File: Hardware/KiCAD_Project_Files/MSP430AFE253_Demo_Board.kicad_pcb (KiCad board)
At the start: 2 copper layers, 25.4 x 50.8 mm, 48 parts, among them J1 USB_MINI_B, P1 POWER, P2 3.3V, P3 Spy-Bi-Wire, P4 TX, P5 RX, P6 GPIO, SW1 FSM4JH, SW2 FSM4JH, SW3 FSM4JH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

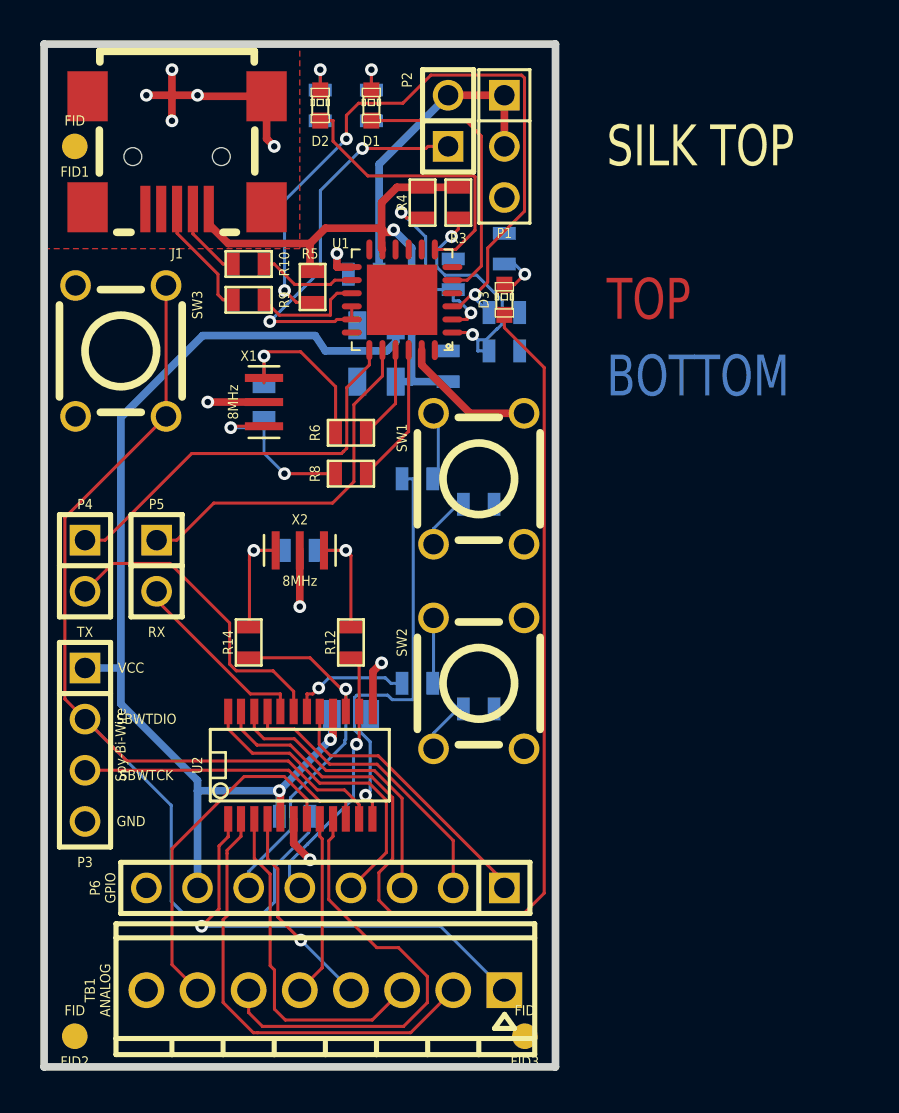
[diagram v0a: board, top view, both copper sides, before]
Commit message: The Freescale USB-to-Serial IC seems to be obsolee.  This is a baseline check-in before changing to the FTDI FT230XQ.
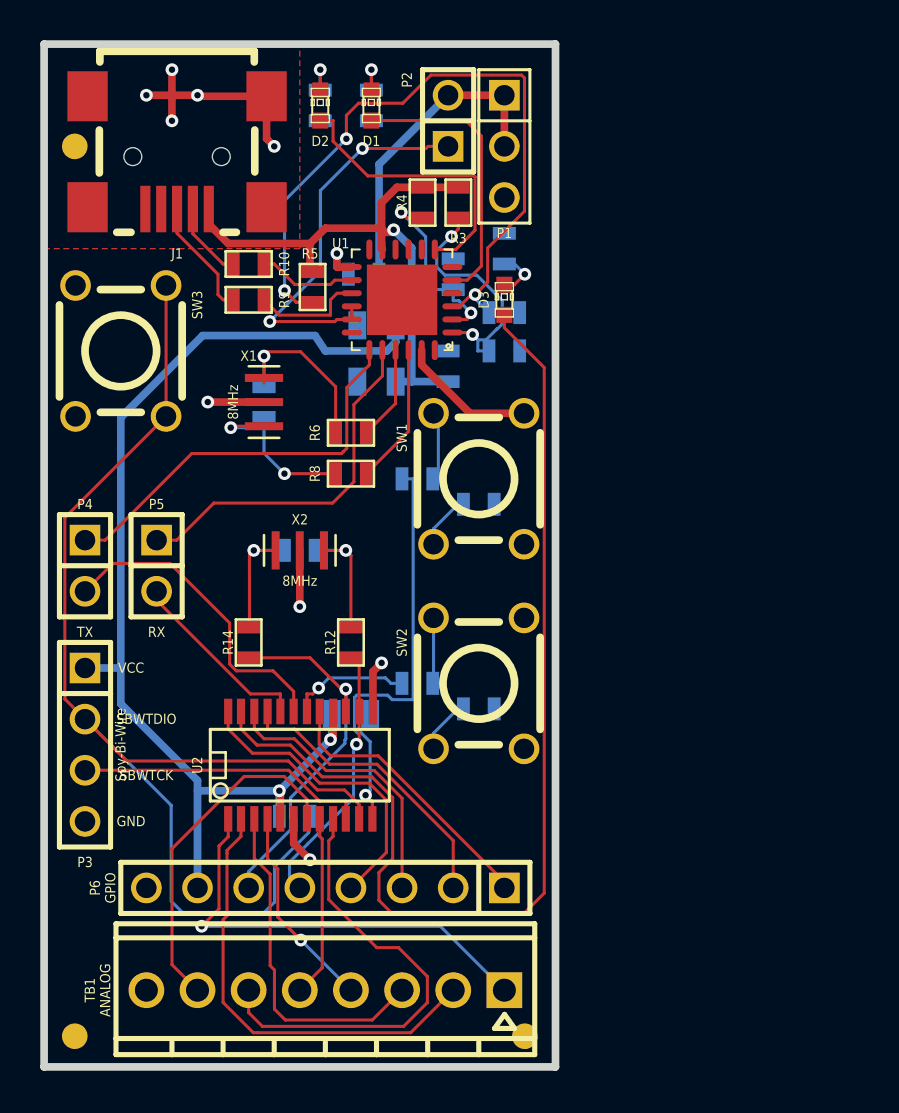
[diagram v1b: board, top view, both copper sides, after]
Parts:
- ?: renamed from FID2; value FID -> (none)
- ?: renamed from FID1; value FID -> (none)
- ?: renamed from FID3; value FID -> (none)
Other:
- board text added: "www.cascologix.com"
- board text removed: "BOTTOM"
- board text removed: "MASK BOTTOM"
- board text removed: "MASK TOP"
- board text removed: "PASTE BOTTOM"
- board text removed: "PASTE TOP"
- board text removed: "SILK BOTTOM"
- board text removed: "SILK TOP"
- board text removed: "TOP"
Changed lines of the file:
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@@
     (links 109)
     (no_connects 1)
-    (area 152.209499 75.5904 197.2564 127.2032)
+    (area 144.078476 70.8152 177.990501 127.2032)
     (thickness 1.6002)
-    (drawings 18)
+    (drawings 11)
     (tracks 448)
     (zones 0)
@@
   )
   (layers
-    (15 Front signal)
+    (15 Front signal hide)
     (0 Back signal)
-    (16 B.Adhes user)
-    (17 F.Adhes user)
-    (18 B.Paste user)
-    (19 F.Paste user)
+    (16 B.Adhes user hide)
+    (17 F.Adhes user hide)
+    (18 B.Paste user hide)
+    (19 F.Paste user hide)
     (20 B.SilkS user)
-    (21 F.SilkS user)
-    (22 B.Mask user)
-    (23 F.Mask user)
+    (21 F.SilkS user hide)
+    (22 B.Mask user hide)
+    (23 F.Mask user hide)
     (24 Dwgs.User user)
     (25 Cmts.User user)
@@
     (aux_axis_origin 152.4 127)
     (grid_origin 152.4 127)
-    (visible_elements FFFFFF7F)
+    (visible_elements 7FFFBFFF)
     (pcbplotparams
       (layerselection 284983297)
@@
     (at 153.924 125.476)
     (path FIDUCIAL)
-    (fp_text reference FID2 (at 0 1.27) (layer F.SilkS)
-      (effects (font (size 0.508 0.4572) (thickness 0.1016)))
-    )
-    (fp_text value FID (at 0 -1.27) (layer F.SilkS)
+    (fp_text reference "" (at 0 1.27) (layer F.SilkS) hide
+      (effects (font (size 0.508 0.4572) (thickness 0.1016)))
+    )
+    (fp_text value "" (at 0 -1.27) (layer F.SilkS) hide
       (effects (font (size 0.508 0.4572) (thickness 0.1016)))
     )
@@
     (at 153.924 81.28)
     (path FIDUCIAL)
-    (fp_text reference FID1 (at 0 1.27) (layer F.SilkS)
-      (effects (font (size 0.508 0.4572) (thickness 0.1016)))
-    )
-    (fp_text value FID (at 0 -1.27) (layer F.SilkS)
+    (fp_text reference "" (at 0 1.27) (layer F.SilkS) hide
+      (effects (font (size 0.508 0.4572) (thickness 0.1016)))
+    )
+    (fp_text value "" (at 0 -1.27) (layer F.SilkS) hide
       (effects (font (size 0.508 0.4572) (thickness 0.1016)))
     )
@@
     (at 176.276 125.476)
     (path FIDUCIAL)
-    (fp_text reference FID3 (at 0 1.27) (layer F.SilkS)
-      (effects (font (size 0.508 0.4572) (thickness 0.1016)))
-    )
-    (fp_text value FID (at 0 -1.27) (layer F.SilkS)
+    (fp_text reference "" (at 0 1.27) (layer F.SilkS) hide
+      (effects (font (size 0.508 0.4572) (thickness 0.1016)))
+    )
+    (fp_text value "" (at 0 -1.27) (layer F.SilkS) hide
       (effects (font (size 0.508 0.4572) (thickness 0.1016)))
     )
@@
     )
   )
+  (gr_text www.cascologix.com (at 161.29 95.885 270) (layer B.SilkS)
+    (effects (font (size 1.27 1.27) (thickness 0.254)) (justify mirror))
+  )
   (dimension 50.8 (width 0.1016) (layer Dwgs.User)
     (gr_text "2.0000 in" (at 147.8788 101.6 270) (layer Dwgs.User)
@@
     (arrow2b (pts (xy 177.8 72.39) (xy 176.673496 72.976421)))
   )
-  (gr_text "PASTE BOTTOM" (at 180.34 104.14) (layer B.Paste)
-    (effects (font (size 2.032 1.524) (thickness 0.3048)) (justify left))
-  )
-  (gr_text "SILK BOTTOM" (at 180.34 100.33) (layer B.SilkS)
-    (effects (font (size 2.032 1.524) (thickness 0.3048)) (justify left))
-  )
-  (gr_text "MASK BOTTOM" (at 180.34 96.52) (layer B.Mask)
-    (effects (font (size 2.032 1.524) (thickness 0.3048)) (justify left))
-  )
-  (gr_text "SILK TOP" (at 180.34 81.28) (layer F.SilkS)
-    (effects (font (size 2.032 1.524) (thickness 0.3048)) (justify left))
-  )
-  (gr_text "MASK TOP" (at 180.34 85.09) (layer F.Mask)
-    (effects (font (size 2.032 1.524) (thickness 0.3048)) (justify left))
-  )
-  (gr_text "PASTE TOP" (at 180.34 77.47) (layer F.Paste)
-    (effects (font (size 2.032 1.524) (thickness 0.3048)) (justify left))
-  )
-  (gr_text TOP (at 180.34 88.9) (layer Front)
-    (effects (font (size 2.032 1.524) (thickness 0.3048)) (justify left))
-  )
-  (gr_text BOTTOM (at 180.34 92.71) (layer Back)
-    (effects (font (size 2.032 1.524) (thickness 0.3048)) (justify left))
-  )
   (gr_text GND (at 156.718 114.808) (layer F.SilkS)

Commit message: One file hadn't been saved prior to the previous check-in.
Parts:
- moved R12 1.80 mm to (167.4, 104.1)
- moved R14 1.80 mm to (162.8, 104.1)
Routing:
- net N-000009: track 6.53 -> 4.64 mm
- net N-000010: track 6.53 -> 4.64 mm
- net XT2IN: track 13.3 -> 15.2 mm
- net N-000032: track 15.8 -> 14.7 mm
- net XT2OUT: track 18.5 -> 19.1 mm

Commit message: Rev 3 release
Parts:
- removed ? (x3): , FIDUCIAL
- removed R4, R5: 47k, SM0603
- removed R6, R8: 0, SM0603
- removed R7: 1M, SM0603
- removed SW3: FSM4JH, SW_TACT_PUSH_6MM_PTH
- removed X1: 8MHz, CER_RES_1.2MM_SMT
- added C11: 0.1u, 0603, F.Cu at (166.4, 112.0)
- added C12: 4.7u, 0603, F.Cu at (166.4, 113.8)
- added C13: 0.1u, 0603, F.Cu at (162.8, 101.9)
- added RST: FSMSM, FSMSM, F.Cu at (154.9, 93.0)
- C1, C10, C2, C5, C6, C9, R1, R11, R13, R15, R16, R17, R2: moved to F.Cu
- C3: value .1u -> 4.7u; moved to F.Cu
- C4, C7, C8: footprint P0805 -> 0603; moved to F.Cu
- P3: value Spy-Bi-Wire -> HEADER_1X4
- P6: value GPIO -> DEBUG
- SW1, SW2: value FSM4JH -> FSMSM; footprint SW_TACT_PUSH_6MM_PTH -> FSMSM
- U1: value USB2SERA10CFK -> FT230XQ; footprint QFN-24_0.65MM -> QFN-16_4MM_0.65MM
- moved C3 27.0 mm to (163.3, 113.8), turned to 180 degrees
- moved C2 26.1 mm to (163.3, 112.0), turned to 180 degrees
- moved P2 25.6 mm to (159.5, 102.1)
- moved C1 16.5 mm to (158.8, 90.7), turned to 180 degrees
- moved R3 16.2 mm to (157.5, 88.8), turned to 180 degrees
- moved C5 13.0 mm to (159.5, 93.2), turned to 270 degrees
- moved R16 11.2 mm to (172.2, 109.0), turned to 90 degrees
- moved C4 11.2 mm to (157.7, 93.2), turned to 270 degrees
- moved R15 8.48 mm to (172.2, 99.6), turned to 270 degrees
- moved C8 8.21 mm to (164.6, 101.9), turned to 90 degrees
- moved U1 7.85 mm to (163.3, 92.7)
- moved C10 6.97 mm to (172.7, 105.9), turned to 90 degrees
- moved C9 6.73 mm to (172.7, 102.6), turned to 270 degrees
- moved C6 5.76 mm to (166.9, 93.2), turned to 90 degrees
- moved R13 4.93 mm to (167.9, 97.3)
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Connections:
- C1 pad 1: N-000030 -> N-0000018
- C10 pad 1: N-000051 -> N-000008
- C2 pad 1: N-000055 -> VCC
- C3 pad 1: N-000029 -> VCC
- C6 pad 1: VCC -> N-0000023
- C7 pad 1: VCC -> N-0000023
- C9 pad 1: N-000049 -> N-0000028
- D1 pad 1: N-000041 -> N-0000015
- D2 pad 1: N-000024 -> N-0000016
- P2 pad 1: N-000053 -> VCC
- P2 pad 2: VCC -> N-0000023
- P4 pad 1: N-000005 (its old number) -> N-0000014
- P5 pad 1: N-000006 (its old number) -> N-0000017
- R10 pad 2: N-000014 -> N-0000021
- R15 pad 2: N-000049 -> N-0000028
- R16 pad 2: N-000051 -> N-000008
- R3 pad 1: N-000030 -> N-0000023
- R3 pad 2: +5V -> N-0000018
- R9 pad 2: N-000013 -> N-0000020
- SW1 pad 1: N-000051 -> N-0000028
- SW1 pad 2: N-000051 -> GND
- SW2 pad 1: N-000049 -> N-000008
- SW2 pad 2: N-000049 -> GND
- U1 pad 1: N-000030 -> N-0000023
- U1 pad 10: (no net) -> +5V
- U1 pad 11: +5V -> N-0000016
- U1 pad 12: (no net) -> N-0000015
- U1 pad 14: N-000014 -> (no net)
- U1 pad 15: N-000013 -> N-0000017
- U1 pad 16: N-000053 -> (no net)
- U1 pad 17: N-000053 -> GND
- U1 pad 2: N-000055 -> N-0000014
- U1 pad 3: N-000029 -> GND
- U1 pad 5: N-000041 -> (no net)
- U1 pad 6: (no net) -> N-0000020
- U1 pad 7: N-000024 -> N-0000021
- U1 pad 8: (no net) -> N-0000023
- U1 pad 9: (no net) -> N-0000018
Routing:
- net VCC: track 75.1 -> 11.5 mm, vias 2 -> 3
- net N-000029: track 35.7 -> 0.00 mm, vias 3 -> 0
- net N-0000029: track 53.7 -> 24.5 mm, vias 0 -> 2
- net N-000004: track 61.5 -> 34.1 mm, vias 0 -> 1
- net N-0000015: track 0.00 -> 25.6 mm, vias 0 -> 2
- net N-0000023: track 0.00 -> 24.0 mm, vias 0 -> 2
- net N-0000014: track 0.00 -> 23.5 mm, vias 0 -> 1
- net N-0000016: track 0.00 -> 23.4 mm, vias 0 -> 2
- net N-000005 (its old number): track 20.2 -> 0.00 mm
- net N-000053: track 19.6 -> 0.00 mm, vias 2 -> 0
- net N-000006 (its old number): track 18.1 -> 0.00 mm
- net +5V: track 29.1 -> 12.9 mm, vias 1 -> 2
- net GND: track 30.5 -> 46.0 mm, vias 10 -> 18
- net N-000006: track 21.3 -> 6.42 mm, vias 1 -> 2
- net N-000024: track 14.5 -> 0.00 mm
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- added copper zone on GND.Cu, net GND
- added copper zone on B.Cu, net NoConnection1
- added copper zone on F.Cu, net NoConnection1
- added copper zone on 3V3.Cu, net VCC
- removed copper zone on B.Cu, net GND
- removed copper zone on F.Cu, net GND
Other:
- copper layers 2 -> 4
- board text added: "3V3"
- board text added: "A0N"
- board text added: "A0P"
- board text added: "A1N"
- board text added: "A1P"
- board text added: "A2N"
- board text added: "A2P"
- board text added: "MSP430AFE253 DEV CASCOLOGIX.COM REV3"
- board text added: "P1.1"
- board text added: "P1.5"
- board text added: "P1.6"
- board text added: "P2.0"
- board text added: "P2.6"
- board text added: "P2.7"
- board text added: "REF"
- board text added: "RX"
- board text added: "TCK"
- board text added: "TDIO"
- board text added: "TX"
- board text removed: "SBWTCK"
- board text removed: "SBWTDIO"
- board text removed: "www.cascologix.com"
